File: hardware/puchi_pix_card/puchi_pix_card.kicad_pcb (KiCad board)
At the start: 4 copper layers, 54 x 54 mm, 370 parts, among them J1 TYPE-C 16P QTWT, J2 SWD XDWF-0910-04P (JST SH com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, Q101 AO3401A, Q102 AO3401A, Q103 AO3401A, Q104 AO3401A, Q105 AO3401A, Q106 AO3401A, Q107 AO3401A, Q108 AO3401A, Q109 AO3401A, Q110 AO3401A, Q111 AO3401A, Q112 AO3401A, Q113 AO3401A, Q114 AO3401A, Q115 AO3401A, Q116 AO3401A, SW1 VBAT_SW, SW2 SW_Push, SW3 SW_Push, U1 TPS61023DRL, U101 MBI5124GP-B (R), U102 MBI5124GP-B (G), U103 MBI5124GP-B (B), U104 74HCT595, U105 74HCT595, U2 XC6206P332MR, U3 STM32G0B1CBTx, U4 XC6206P332MR, U5 USBLC6-2SC6, U6 KXTJ3-1057, U7 W25Q64JVSSIQ

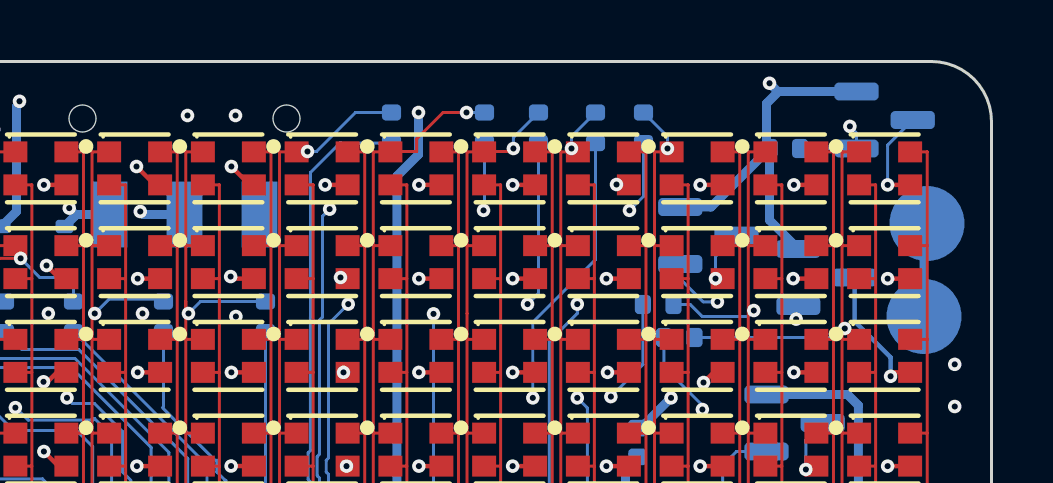
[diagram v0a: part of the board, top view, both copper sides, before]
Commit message: Relink BT1/BT2 footprints to their schematic symbols and restore the battery route to SW1/C1; firmware checks VBUS before enabling the boost now that VIN stays on the battery
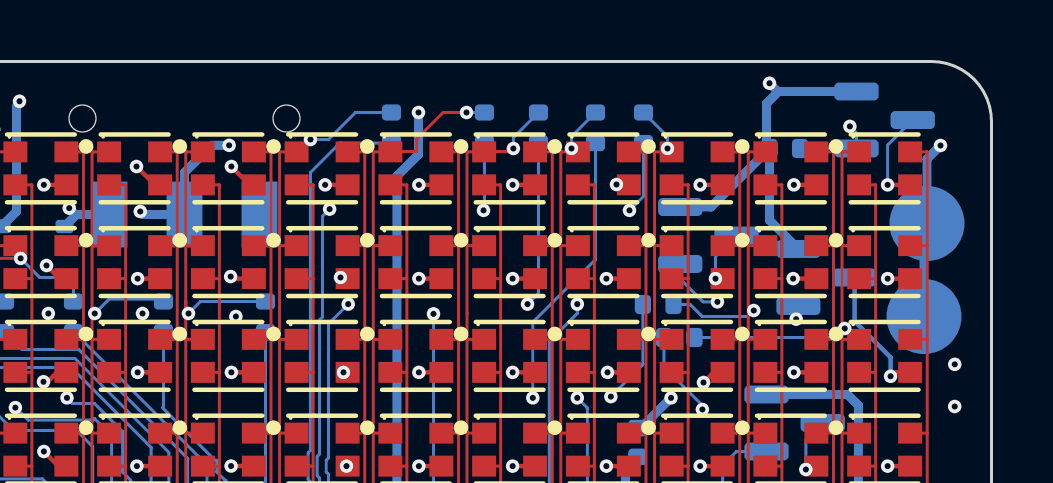
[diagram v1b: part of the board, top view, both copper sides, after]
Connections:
- BT1 pad 1: VBAT -> Net-(BT1-Pin_1)
- BT2 pad 1: VBAT -> Net-(BT1-Pin_1)
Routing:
- net Net-(BT1-Pin_1): track 27.9 -> 62.6 mm, vias 3 -> 5
- net VBAT: track 3.14 -> 0.00 mm
- net SR_SRCLK: track 100.2 -> 100.0 mm, vias 4 -> 2

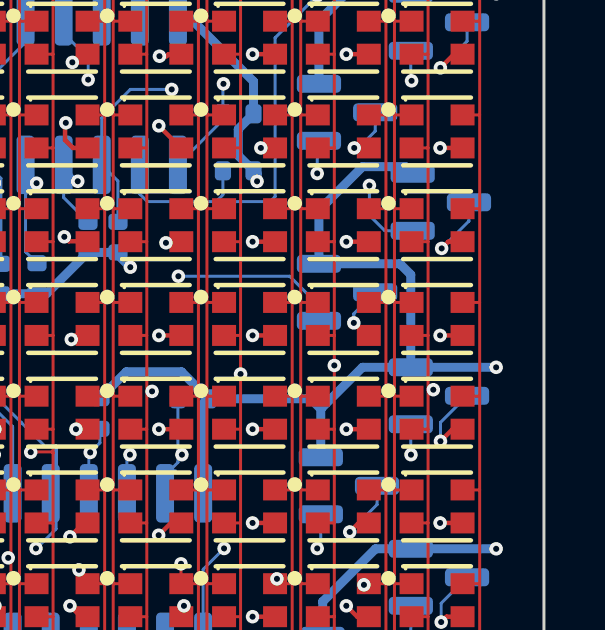
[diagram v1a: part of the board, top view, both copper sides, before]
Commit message: Add C106 10uF bulk capacitor on +5V next to the row PFET column (row switching transient, USB headroom)
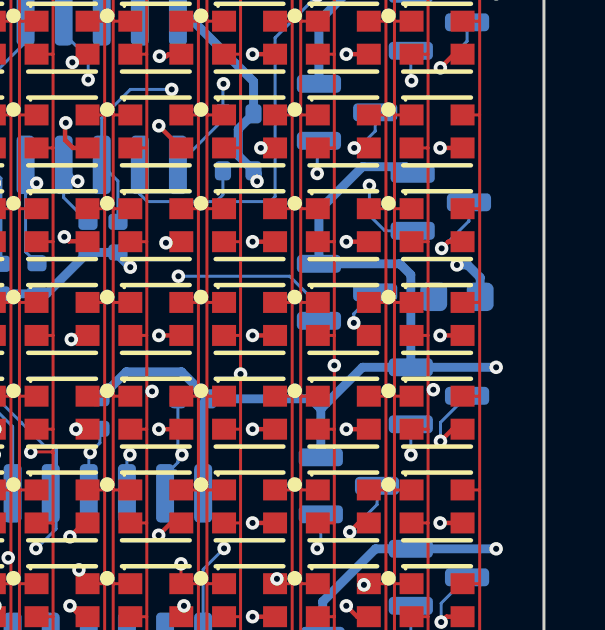
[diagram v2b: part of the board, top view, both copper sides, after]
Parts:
- added C106: 10uF, Capacitor_SMD:C_0603_1608Metric, B.Cu at (151.1, 124.7)
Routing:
- net GND: track 152.0 -> 153.6 mm, vias 23 -> 24
- net +5V: track 430.2 -> 430.9 mm
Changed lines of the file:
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@@
 		)
 	)
+	(footprint "Capacitor_SMD:C_0603_1608Metric"
+		(layer "B.Cu")
+		(at 151.1 124.7)
+		(descr "Capacitor SMD 0603 (1608 Metric), square (rectangular) end terminal, IPC-7351 nominal, (Body size source: IPC-SM-782 page 76, https://www.pcb-3d.com/wordpress/wp-content/uploads/ipc-sm-782a_amendment_1_and_2.pdf), generated with kicad-footprint-generator")
+		(tags "capacitor")
+		(property "Reference" "C106"
+			(at 0 1.43 180)
+			(layer "B.SilkS")
+			(hide yes)
+			(effects
+				(font
+					(size 1 1)
+					(thickness 0.15)
+				)
+				(justify mirror)
+			)
+		)
+		(property "Value" "10uF"
+			(at 0 -1.43 180)
+			(layer "B.Fab")
+			(hide yes)
+			(effects
+				(font
+					(size 1 1)
+					(thickness 0.15)
+				)
+				(justify mirror)
+			)
+		)
+		(property "Datasheet" ""
+			(at 0 0 180)
+			(layer "B.Fab")
+			(hide yes)
+			(effects
+				(font
+					(size 1.27 1.27)
+					(thickness 0.15)
+				)
+				(justify mirror)
+			)
+		)
+		(property "Description" ""
+			(at 0 0 180)
+			(layer "B.Fab")
+			(hide yes)
+			(effects
+				(font
+					(size 1.27 1.27)
+					(thickness 0.15)
+				)
+				(justify mirror)
+			)
+		)
+		(attr smd)
+		(fp_line
+			(start -0.14058 -0.51)
+			(end 0.14058 -0.51)
+			(stroke
+				(width 0.12)
+				(type solid)
+			)
+			(layer "B.SilkS")
+		)
+		(fp_line
+			(start -0.14058 0.51)
+			(end 0.14058 0.51)
+			(stroke
+				(width 0.12)
+				(type solid)
+			)
+			(layer "B.SilkS")
+		)
+		(fp_rect
+			(start -1.48 0.73)
+			(end 1.48 -0.73)
+			(stroke
+				(width 0.05)
+				(type solid)
+			)
+			(fill no)
+			(layer "B.CrtYd")
+		)
+		(fp_rect
+			(start -0.8 0.4)
+			(end 0.8 -0.4)
+			(stroke
+				(width 0.1)
+				(type solid)
+			)
+			(fill no)
+			(layer "B.Fab")
+		)
+		(fp_text user "${REFERENCE}"
+			(at 0 0 180)
+			(layer "B.Fab")
+			(effects
+				(font
+					(size 0.4 0.4)
+					(thickness 0.06)
+				)
+				(justify mirror)
+			)
+		)
+		(pad "1" smd roundrect
+			(at -0.775 0)
+			(size 0.9 0.95)
+			(layers "B.Cu" "B.Mask" "B.Paste")
+			(roundrect_rratio 0.25)
+			(net 3 "+5V")
+		)
+		(pad "2" smd roundrect
+			(at 0.775 0)
+			(size 0.9 0.95)
+			(layers "B.Cu" "B.Mask" "B.Paste")
+			(roundrect_rratio 0.25)
+			(net 2 "GND")
+		)
+		(embedded_fonts no)
+		(model "${KICAD9_3DMODEL_DIR}/Capacitor_SMD.3dshapes/C_0603_1608Metric.step"
+			(offset
+				(xyz 0 0 0)
+			)
+			(scale
+				(xyz 1 1 1)
+			)
+			(rotate
+				(xyz 0 0 0)
+			)
+		)
+	)
 	(footprint "Capacitor_SMD:C_0402_1005Metric"
 		(layer "B.Cu")
@@
 	)
 	(via
+		(at 151.1 123.637502)
+		(size 0.45)
+		(drill 0.2)
+		(layers "F.Cu" "B.Cu")
+		(net 2)
+	)
+	(via
 		(at 118.3175 120.912498)
 		(size 0.45)
@@
 	)
 	(segment
+		(start 151.1 123.637502)
+		(end 151.455002 123.637502)
+		(width 0.3)
+		(layer "B.Cu")
+		(net 2)
+	)
+	(segment
 		(start 110.3 148.2)
 		(end 108.33 148.2)
@@
 	)
 	(segment
+		(start 151.875 124.0575)
+		(end 151.875 124.7)
+		(width 0.3)
+		(layer "B.Cu")
+		(net 2)
+	)
+	(segment
 		(start 128.48 130.32)
 		(end 128.48 131.08)
@@
 	)
 	(segment
+		(start 151.455002 123.637502)
+		(end 151.875 124.0575)
+		(width 0.3)
+		(layer "B.Cu")
+		(net 2)
+	)
+	(segment
 		(start 133.75 136.2)
 		(end 133.75 133.3385)
@@
 	)
 	(segment
+		(start 149.5625 124.7)
+		(end 150.325 124.7)
+		(width 0.3)
+		(layer "B.Cu")
+		(net 3)
+	)
+	(segment
 		(start 146.875 101)
 		(end 146.6 100.725)
@@
 	)
 	(segment
+		(start 149.5625 124.7)
+		(end 149.5625 123.9625)
+		(width 0.3)
+		(layer "B.Cu")
+		(net 3)
+	)
+	(segment
 		(start 146.5 111.1)
 		(end 149.2 111.1)
@@
 	(segment
 		(start 149.5625 127.05)
-		(end 149.5625 123.9625)
+		(end 149.5625 124.7)
 		(width 0.3)
 		(layer "B.Cu")
